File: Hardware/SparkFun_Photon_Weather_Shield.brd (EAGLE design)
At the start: 66 x 35.6 mm, 44 parts, among them U1 3.3V MIC5219, U2 HTU21D, U3 MPL3115A2LGA8

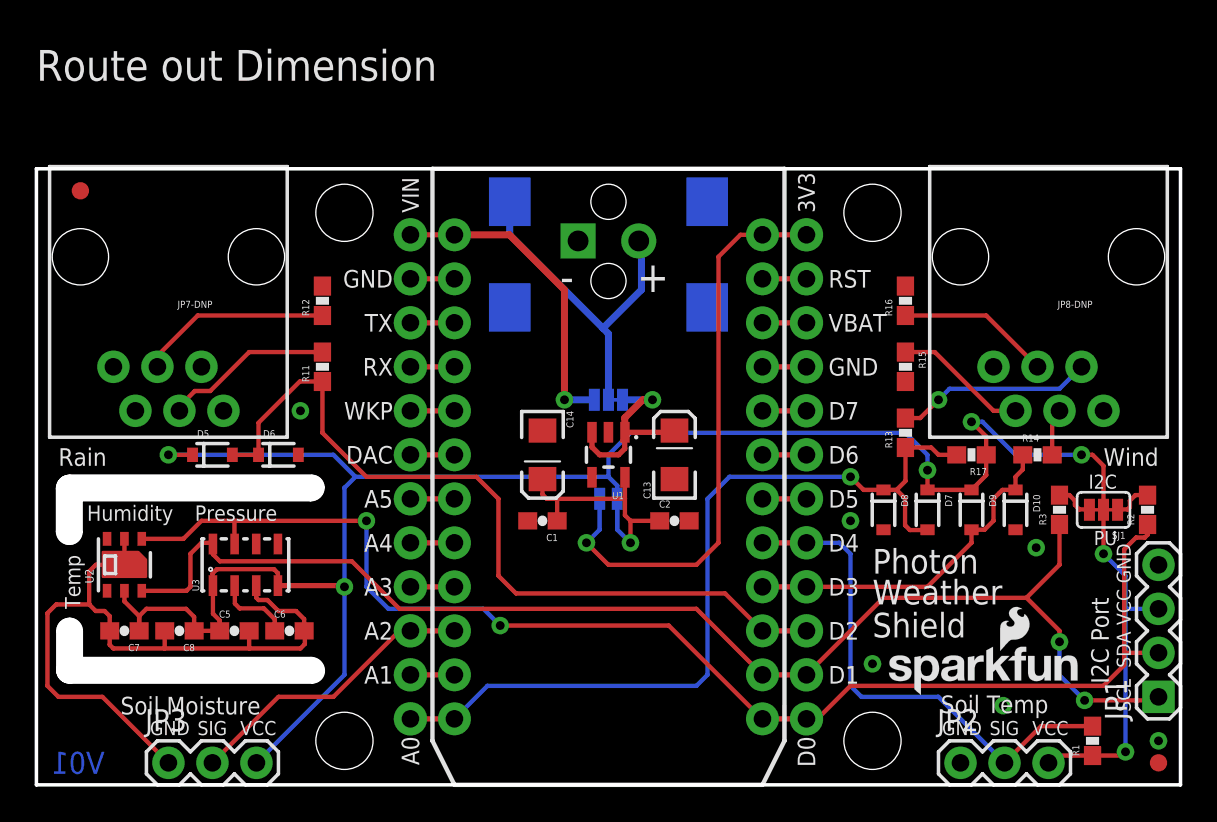
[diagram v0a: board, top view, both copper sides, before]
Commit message: QC Checklist Issues Addressed
QC Checklist Issues Addressed: added PROD_IDs to few missing parts,
changed Y junctions to T junctions, fixed pin 1 markings, added Values
where needed.
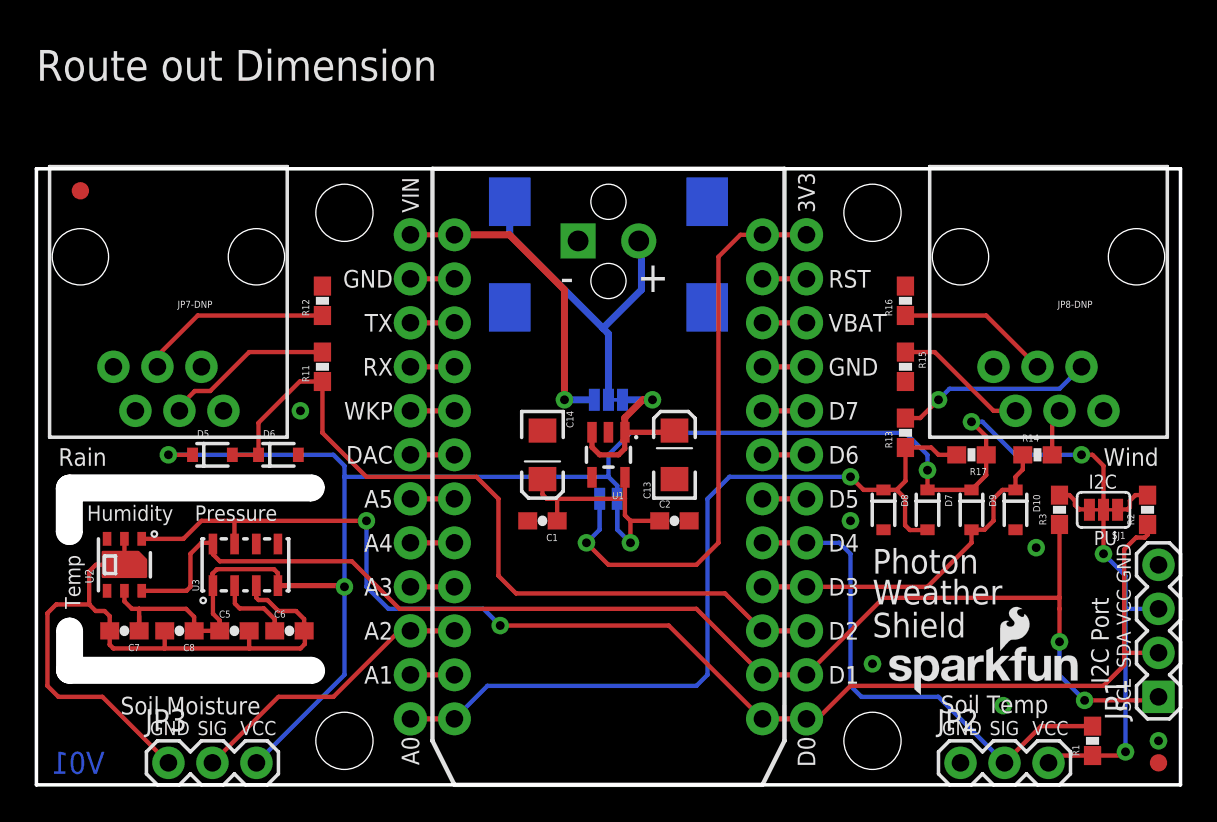
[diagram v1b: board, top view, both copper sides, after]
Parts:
- JP1: value (none) -> I2C Port
- JP2: value (none) -> Soil/Water Temp
- JP3: value (none) -> Soil Moisture
- JP6: value M023.5MM -> (none)
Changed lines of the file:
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@@
 <layer number="47" name="Measures" color="7" fill="1" visible="no" active="yes"/>
 <layer number="48" name="Document" color="7" fill="1" visible="no" active="yes"/>
-<layer number="49" name="Reference" color="7" fill="1" visible="no" active="yes"/>
+<layer number="49" name="Reference" color="7" fill="1" visible="yes" active="yes"/>
 <layer number="50" name="dxf" color="7" fill="1" visible="no" active="no"/>
 <layer number="51" name="tDocu" color="6" fill="1" visible="yes" active="yes"/>
@@
 <attribute name="VALUE" value="1.0uF" x="29.21" y="15.24" size="1.778" layer="27" rot="R180" display="off"/>
 </element>
-<element name="U3" library="SparkFun-Sensors" package="LGA8" value="MPL3115A2LGA8" x="12.065" y="12.7" rot="R90"/>
+<element name="U3" library="SparkFun-Sensors" package="LGA8" value="MPL3115A2LGA8" x="12.065" y="12.7" rot="R90">
+<attribute name="PROD_ID" value="IC-10869" x="12.065" y="12.7" size="1.778" layer="27" rot="R90" display="off"/>
+</element>
 <element name="C7" library="SparkFun-Capacitors" package="0603-CAP" value="0.1uF" x="5.08" y="8.89" rot="R180">
 <attribute name="PROD_ID" value="CAP-00810" x="5.08" y="8.89" size="1.778" layer="27" rot="R180" display="off"/>
@@
 <attribute name="VALUE" value="0.1uF" x="11.43" y="8.89" size="1.778" layer="27" display="off"/>
 </element>
-<element name="U2" library="SparkFun-Sensors" package="HTU21D" value="HTU21D" x="5.08" y="12.7" rot="R90"/>
+<element name="U2" library="SparkFun-Sensors" package="HTU21D" value="HTU21D" x="5.08" y="12.7" rot="R90">
+<attribute name="PROD_ID" value="IC-11793" x="5.08" y="12.7" size="1.778" layer="27" rot="R90" display="off"/>
+</element>
 <element name="C13" library="SparkFun-Capacitors" package="EIA3216" value="10uF" x="36.83" y="19.05" rot="R90">
 <attribute name="PROD_ID" value="CAP-00811" x="36.83" y="19.05" size="1.778" layer="27" rot="R90" display="off"/>
@@
 </element>
 <element name="LOGO1" library="SparkFun-Aesthetics" package="OSHW-LOGO-M" value="OSHW-LOGOM" x="54.61" y="12.065" rot="MR0"/>
-<element name="JP2" library="SparkFun-Connectors" package="1X03" value="" x="53.34" y="1.27"/>
-<element name="JP3" library="SparkFun-Connectors" package="1X03" value="" x="7.62" y="1.27"/>
+<element name="JP2" library="SparkFun-Connectors" package="1X03" value="Soil/Water Temp" x="53.34" y="1.27"/>
+<element name="JP3" library="SparkFun-Connectors" package="1X03" value="Soil Moisture" x="7.62" y="1.27"/>
 <element name="R1" library="SparkFun-Resistors" package="0603-RES" value="4.7K" x="60.96" y="2.54" rot="R90">
 <attribute name="PROD_ID" value="RES-07857" x="60.96" y="2.54" size="1.778" layer="27" font="vector" ratio="15" rot="R90" display="off"/>
 </element>
 <element name="JP4" library="template_temp" package="SPARK_PHOTON_TEMPLATE" value="SPARK_PHOTONTEMPLATE" x="22.86" y="0"/>
-<element name="JP1" library="SparkFun-Connectors" package="1X04" value="" x="64.77" y="5.08" rot="R90"/>
+<element name="JP1" library="SparkFun-Connectors" package="1X04" value="I2C Port" x="64.77" y="5.08" rot="R90"/>
 <element name="SJ1" library="SparkFun-Passives" package="PAD-JUMPER-3-3OF3_NC_BY_TRACE_YES_SILK_FULL_BOX" value="" x="61.595" y="15.875" rot="R180"/>
 <element name="R2" library="SparkFun-Resistors" package="0603-RES" value="10K" x="64.135" y="15.875" rot="R90">
@@
 <element name="JP5" library="SparkFun-Connectors" package="POWER_JACK_SMD" value="5.5x2.1mm Barrel" x="33.02" y="33.655" rot="MR270">
 <attribute name="PROD_ID" value="CONN-08106" x="33.02" y="33.655" size="1.778" layer="28" font="vector" ratio="15" rot="MR270" display="off"/>
-</element>
-<element name="JP6" library="SparkFun-Connectors" package="SCREWTERMINAL-3.5MM-2" value="M023.5MM" x="31.2674" y="31.3944" rot="MR180">
+<attribute name="SF_ID" value="PRT-12748" x="33.02" y="33.655" size="1.778" layer="28" rot="MR270" display="off"/>
+</element>
+<element name="JP6" library="SparkFun-Connectors" package="SCREWTERMINAL-3.5MM-2" value="" x="31.2674" y="31.3944" rot="MR180">
 <attribute name="PROD_ID" value="CONN-08399" x="31.2674" y="31.3944" size="1.778" layer="28" font="vector" ratio="15" rot="MR180" display="off"/>
 </element>
@@
 <wire x1="10.16" y1="12.192" x2="10.16" y2="11.53" width="0.254" layer="1"/>
 <wire x1="10.16" y1="11.53" x2="10.19" y2="11.5" width="0.254" layer="1"/>
-<wire x1="5.08" y1="10.5918" x2="5.93" y2="9.7418" width="0.254" layer="1"/>
-<wire x1="5.93" y1="9.7418" x2="5.93" y2="8.89" width="0.254" layer="1"/>
+<wire x1="5.93" y1="10.16" x2="5.93" y2="8.89" width="0.254" layer="1"/>
 <wire x1="13.94" y1="11.5" x2="13.94" y2="12.222" width="0.254" layer="1"/>
 <contactref element="JP2" pad="3"/>
@@
 <wire x1="58.84" y1="1.69" x2="58.42" y2="1.27" width="0.254" layer="1"/>
 <wire x1="35.98" y1="15.24" x2="36.0172" y2="15.2028" width="0.254" layer="1"/>
-<wire x1="18.415" y1="17.78" x2="33.02" y2="17.78" width="0.254" layer="16"/>
+<wire x1="17.78" y1="17.78" x2="33.02" y2="17.78" width="0.254" layer="16"/>
 <wire x1="54.825" y1="19.05" x2="54.825" y2="17.875" width="0.254" layer="1"/>
 <wire x1="54.825" y1="17.875" x2="53.975" y2="17.025" width="0.254" layer="1"/>
@@
 <via x="34.29" y="13.97" extent="1-16" drill="0.508"/>
 <wire x1="34.29" y1="13.97" x2="34.29" y2="15.24" width="0.254" layer="1"/>
-<wire x1="17.78" y1="11.43" x2="17.78" y2="17.145" width="0.254" layer="16"/>
-<wire x1="17.78" y1="17.145" x2="18.415" y2="17.78" width="0.254" layer="16"/>
-<wire x1="18.415" y1="17.78" x2="17.145" y2="19.05" width="0.254" layer="16"/>
+<wire x1="17.78" y1="11.43" x2="17.78" y2="17.78" width="0.254" layer="16"/>
+<wire x1="17.78" y1="17.78" x2="17.78" y2="18.415" width="0.254" layer="16"/>
 <wire x1="33.528" y1="16.51" x2="33.528" y2="17.272" width="0.254" layer="16"/>
 <wire x1="33.528" y1="17.272" x2="33.02" y2="17.78" width="0.254" layer="16"/>
@@
 <wire x1="17.78" y1="6.35" x2="17.78" y2="11.43" width="0.254" layer="16"/>
 <wire x1="5.93" y1="8.89" x2="5.93" y2="9.74" width="0.254" layer="1"/>
-<wire x1="5.93" y1="9.74" x2="6.35" y2="10.16" width="0.254" layer="1"/>
-<wire x1="6.35" y1="10.16" x2="8.636" y2="10.16" width="0.254" layer="1"/>
+<wire x1="5.5118" y1="10.16" x2="5.93" y2="10.16" width="0.254" layer="1"/>
+<wire x1="5.93" y1="10.16" x2="8.636" y2="10.16" width="0.254" layer="1"/>
 <wire x1="8.636" y1="10.16" x2="9.105" y2="9.691" width="0.254" layer="1"/>
 <wire x1="9.105" y1="9.691" x2="9.105" y2="8.89" width="0.254" layer="1"/>
+<wire x1="5.5118" y1="10.16" x2="5.08" y2="10.5918" width="0.254" layer="1"/>
+<wire x1="17.78" y1="18.415" x2="17.145" y2="19.05" width="0.254" layer="16"/>
 </signal>
 <signal name="SCL">
@@
 <via x="60.5028" y="4.8768" extent="1-16" drill="0.508"/>
 <via x="59.055" y="8.255" extent="1-16" drill="0.508"/>
-<wire x1="59.055" y1="8.255" x2="59.055" y2="8.89" width="0.254" layer="1"/>
 <wire x1="59.055" y1="8.255" x2="59.055" y2="6.3246" width="0.254" layer="16"/>
 <wire x1="64.77" y1="5.08" x2="64.5668" y2="4.8768" width="0.254" layer="1"/>
@@
 <wire x1="10.5918" y1="12.9032" x2="18.2118" y2="12.9032" width="0.254" layer="1"/>
 <wire x1="18.2118" y1="12.9032" x2="20.955" y2="10.16" width="0.254" layer="1"/>
-<wire x1="57.15" y1="10.795" x2="48.895" y2="10.795" width="0.254" layer="1"/>
+<wire x1="59.055" y1="10.795" x2="48.895" y2="10.795" width="0.254" layer="1"/>
 <wire x1="48.895" y1="10.795" x2="44.45" y2="6.35" width="0.254" layer="1"/>
-<wire x1="57.15" y1="10.795" x2="59.055" y2="8.89" width="0.254" layer="1"/>
-<wire x1="59.055" y1="15.025" x2="59.055" y2="12.7" width="0.254" layer="1"/>
-<wire x1="59.055" y1="12.7" x2="57.15" y2="10.795" width="0.254" layer="1"/>
 <wire x1="38.1" y1="10.16" x2="41.91" y2="6.35" width="0.254" layer="1"/>
+<wire x1="59.055" y1="8.255" x2="59.055" y2="10.16" width="0.254" layer="1"/>
+<wire x1="59.055" y1="10.795" x2="59.055" y2="15.025" width="0.254" layer="1"/>
+<wire x1="59.055" y1="10.795" x2="59.055" y2="10.16" width="0.254" layer="1"/>
 </signal>
 <signal name="SDA">

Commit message: Added DNP to a few connectors
Added DNP to a few connectors that I missed and do not need to be
populated.
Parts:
- renumbered JP5 to JP5-DNP, JP6 to JP6-DNP
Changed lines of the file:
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@@
 <attribute name="PROD_ID" value="RES-00824" x="59.055" y="15.875" size="1.778" layer="27" font="vector" ratio="15" rot="R90" display="off"/>
 </element>
-<element name="JP5" library="SparkFun-Connectors" package="POWER_JACK_SMD" value="5.5x2.1mm Barrel" x="33.02" y="33.655" rot="MR270">
+<element name="JP5-DNP" library="SparkFun-Connectors" package="POWER_JACK_SMD" value="5.5x2.1mm Barrel" x="33.02" y="33.655" rot="MR270">
 <attribute name="PROD_ID" value="CONN-08106" x="33.02" y="33.655" size="1.778" layer="28" font="vector" ratio="15" rot="MR270" display="off"/>
 <attribute name="SF_ID" value="PRT-12748" x="33.02" y="33.655" size="1.778" layer="28" rot="MR270" display="off"/>
 </element>
-<element name="JP6" library="SparkFun-Connectors" package="SCREWTERMINAL-3.5MM-2" value="" x="31.2674" y="31.3944" rot="MR180">
+<element name="JP6-DNP" library="SparkFun-Connectors" package="SCREWTERMINAL-3.5MM-2" value="" x="31.2674" y="31.3944" rot="MR180">
 <attribute name="PROD_ID" value="CONN-08399" x="31.2674" y="31.3944" size="1.778" layer="28" font="vector" ratio="15" rot="MR180" display="off"/>
 </element>
@@
 <contactref element="JP4" pad="GND@2"/>
 <contactref element="JP1" pad="4"/>
-<contactref element="JP5" pad="GND"/>
-<contactref element="JP5" pad="P$4"/>
-<contactref element="JP6" pad="1"/>
+<contactref element="JP5-DNP" pad="GND"/>
+<contactref element="JP5-DNP" pad="P$4"/>
+<contactref element="JP6-DNP" pad="1"/>
 <via x="46.99" y="15.24" extent="1-16" drill="0.508"/>
 <via x="64.77" y="2.54" extent="1-16" drill="0.508"/>
@@
 </signal>
 <signal name="RAW" class="1">
-<contactref element="JP5" pad="VIN0"/>
-<contactref element="JP6" pad="2"/>
+<contactref element="JP5-DNP" pad="VIN0"/>
+<contactref element="JP6-DNP" pad="2"/>
 <contactref element="SJ2" pad="2"/>
 <wire x1="34.925" y1="28.575" x2="34.925" y2="31.2368" width="0.4064" layer="16"/>

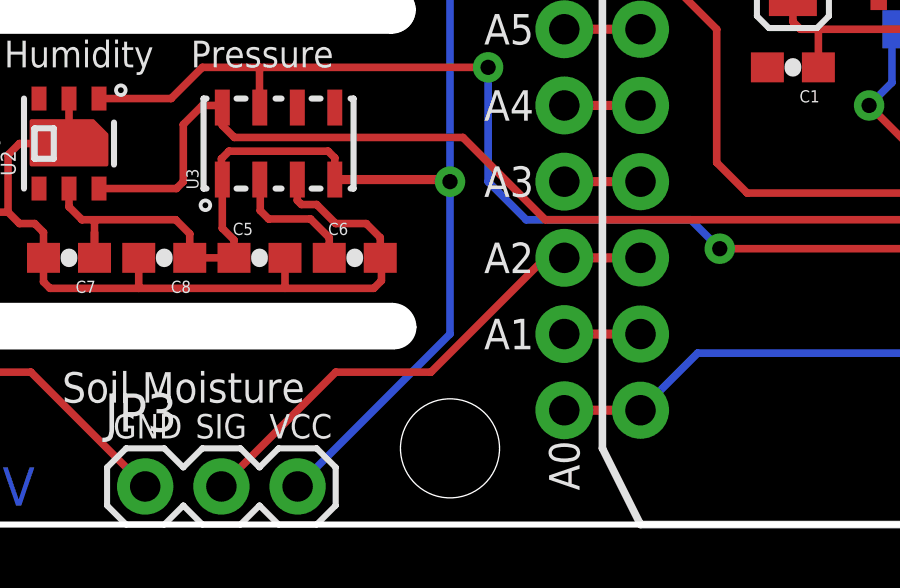
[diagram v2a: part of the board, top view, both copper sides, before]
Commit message: Ready for Protos
Moved Soil_Moisture from A2 to A1 and deleted unused Light  net on A1.
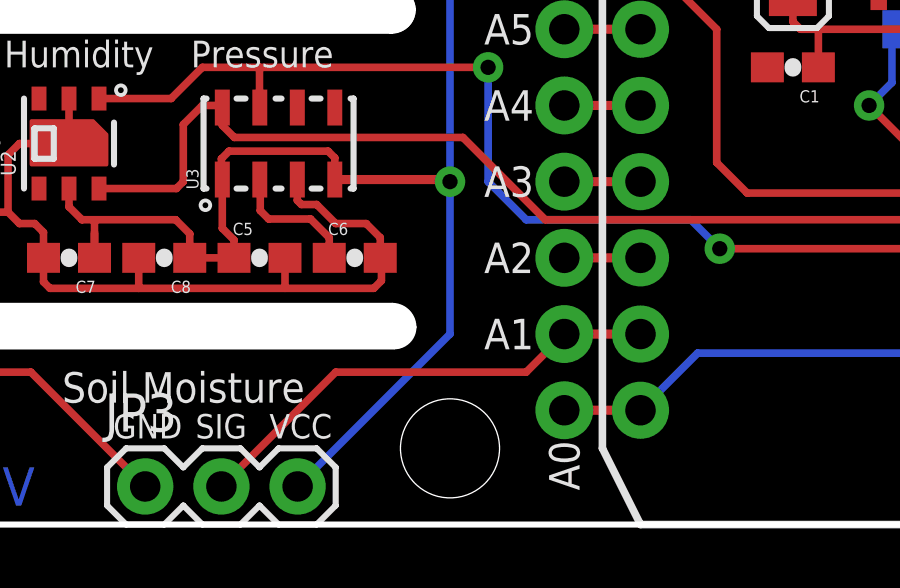
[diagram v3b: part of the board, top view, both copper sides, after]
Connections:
- removed net LIGHT: JP4.11, JP4.A1
- net SOIL_MOIST: now also JP4.11, JP4.A1; no longer JP4.10, JP4.A2
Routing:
- net SOIL_MOIST: track 14.6 -> 13.5 mm
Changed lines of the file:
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@@
 <layer number="47" name="Measures" color="7" fill="1" visible="no" active="yes"/>
 <layer number="48" name="Document" color="7" fill="1" visible="no" active="yes"/>
-<layer number="49" name="Reference" color="7" fill="1" visible="yes" active="yes"/>
+<layer number="49" name="Reference" color="7" fill="1" visible="no" active="yes"/>
 <layer number="50" name="dxf" color="7" fill="1" visible="no" active="no"/>
 <layer number="51" name="tDocu" color="6" fill="1" visible="yes" active="yes"/>
@@
 <wire x1="13.755" y1="9.5622" x2="13.755" y2="8.89" width="0.254" layer="1"/>
 </signal>
-<signal name="LIGHT">
-<contactref element="JP4" pad="A1"/>
-<contactref element="JP4" pad="11"/>
-</signal>
 <signal name="RAIN">
 <contactref element="R11" pad="1"/>
@@
 <signal name="SOIL_MOIST">
 <contactref element="JP3" pad="2"/>
-<contactref element="JP4" pad="A2"/>
-<contactref element="JP4" pad="10"/>
-<wire x1="20.955" y1="8.89" x2="21.59" y2="8.89" width="0.254" layer="1"/>
-<wire x1="17.145" y1="5.08" x2="20.955" y2="8.89" width="0.254" layer="1"/>
-<wire x1="17.145" y1="5.08" x2="13.97" y2="5.08" width="0.254" layer="1"/>
 <wire x1="13.97" y1="5.08" x2="10.16" y2="1.27" width="0.254" layer="1"/>
+<contactref element="JP4" pad="11"/>
+<contactref element="JP4" pad="A1"/>
+<wire x1="13.97" y1="5.08" x2="20.32" y2="5.08" width="0.254" layer="1"/>
+<wire x1="20.32" y1="5.08" x2="21.59" y2="6.35" width="0.254" layer="1"/>
 </signal>
 <signal name="TXO">
